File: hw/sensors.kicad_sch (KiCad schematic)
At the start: 0 parts

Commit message: working on documentation, design methmethodology, sizing, layout
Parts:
- added C401, C402, C403, C404: 100nF, Capacitor_SMD:C_0805_2012Metric, symbol Device:C_Small
- added D401, D402, D403, D404: 3.3V Zener, Diode_SMD:D_MiniMELF, symbol Device:D_Zener_Small
- added R401, R402: 2m, Resistor_SMD:R_1206_3216Metric, symbol Device:R
- added R403, R405: 100k, Resistor_SMD:R_0805_2012Metric, symbol Device:R
- added R404: 3k, Resistor_SMD:R_0805_2012Metric, symbol Device:R
- added R406: 2k, Resistor_SMD:R_0805_2012Metric, symbol Device:R
- added TP401, TP405: GND, TestPoint:TestPoint_Pad_1.0x1.0mm, symbol Connector:TestPoint
- added TP402: -ARR, TestPoint:TestPoint_Pad_1.0x1.0mm, symbol Connector:TestPoint
- added TP403: Array Current, TestPoint:TestPoint_Pad_1.0x1.0mm, symbol Connector:TestPoint
- added TP404: -BATT, TestPoint:TestPoint_Pad_1.0x1.0mm, symbol Connector:TestPoint
- added TP406: Battery Current, TestPoint:TestPoint_Pad_1.0x1.0mm, symbol Connector:TestPoint
- added TP407: +ARR, TestPoint:TestPoint_Pad_1.0x1.0mm, symbol Connector:TestPoint
- added TP408: Array Voltage, TestPoint:TestPoint_Pad_1.0x1.0mm, symbol Connector:TestPoint
- added TP409: +BATT, TestPoint:TestPoint_Pad_1.0x1.0mm, symbol Connector:TestPoint
- added TP410: Battery Voltage, TestPoint:TestPoint_Pad_1.0x1.0mm, symbol Connector:TestPoint
- added U401, U402: INA210, Package_TO_SOT_SMD:SOT-363_SC-70-6_Handsoldering, symbol MPPT:OP_AMP_INA21x
- added U403, U404: OPA990, Package_TO_SOT_SMD:SOT-23-6, symbol Amplifier_Operational:MAX4238AUT
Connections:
- new net: R403.1, R404.1, U403.3 (+)
- new net: R405.1, R406.1, U404.3 (+)
- new net +12V: C401.2, C402.2, C403.2, C404.2, U401.3 (V+), U402.3 (V+), U403.6 (V+), U404.6 (V+)
- new net +ARR: R403.2, TP407.1
- new net +BATT: R405.2, TP409.1
- new net -ARR: R401.1, TP402.1, U401.5 (-)
- new net -BATT: R402.2, TP404.1, U402.4 (+)
- new net ARRAY_CURRENT: D401.1 (K), TP403.1, U401.6
- new net ARRAY_VOLTAGE: D403.1 (K), TP408.1, U403.1, U403.4 (-)
- new net BATTERY_CURRENT: D402.1 (K), TP406.1, U402.6
- new net BATTERY_VOLTAGE: D404.1 (K), TP410.1, U404.1, U404.4 (-)
- new net GND: C401.1, C402.1, C403.1, C404.1, D401.2 (A), D402.2 (A), D403.2 (A), D404.2 (A), R401.2, R402.1, R404.2, R406.2, TP401.1, TP405.1, U401.1 (REF), U401.2 (V-), U401.4 (+), U402.1 (REF), U402.2 (V-), U402.5 (-), U403.2 (V-), U403.5 (~{SHDN}), U404.2 (V-), U404.5 (~{SHDN})
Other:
- note added: "0-100V"
- note added: "0-150V"
- note added: "0-3V"
- note added: "7.5A 0-15mV"
- note added: "Array Current Sensor"
- note added: "Array Voltage Sensor"
- note added: "Battery Current Sensor"
- note added: "Battery Voltage Sensor"

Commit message: slight bom updates
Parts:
- C401, U401, U402: In Stock? (none) -> Y
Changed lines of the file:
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@@
+      (effects (font (size 1.27 1.27)) hide)
+    )
+    (property "In Stock?" "Y" (at 69.85 96.52 0)
       (effects (font (size 1.27 1.27)) hide)
     )
@@
       (effects (font (size 1.27 1.27)) hide)
     )
+    (property "In Stock?" "Y" (at 125.73 96.52 0)
+      (effects (font (size 1.27 1.27)) hide)
+    )
     (pin "1")
     (pin "2")
@@
       (effects (font (size 1 1)) hide)
     )
-    (pin "1")
+    (property "In Stock?" "Y" (at 80.01 85.09 0)
+      (effects (font (size 1.27 1.27)) hide)
+    )
+    (pin "1")

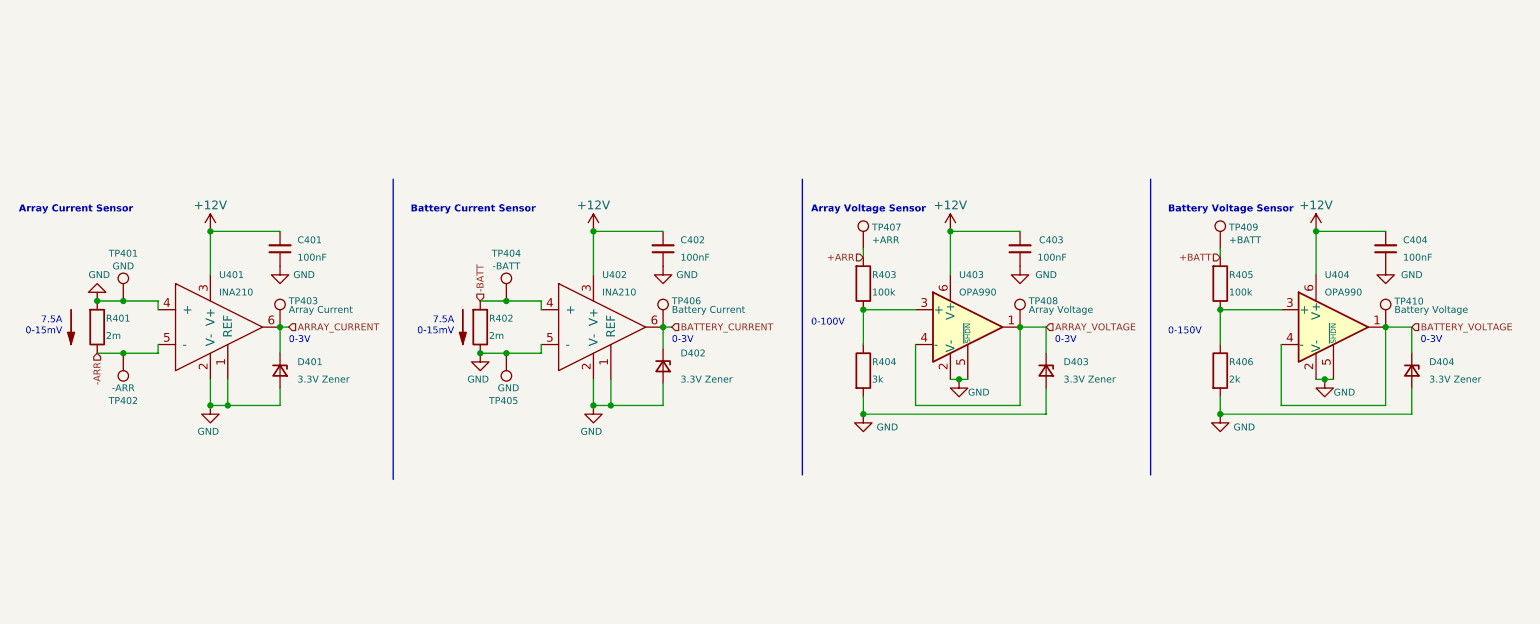
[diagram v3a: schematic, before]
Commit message: revision of PCB layout
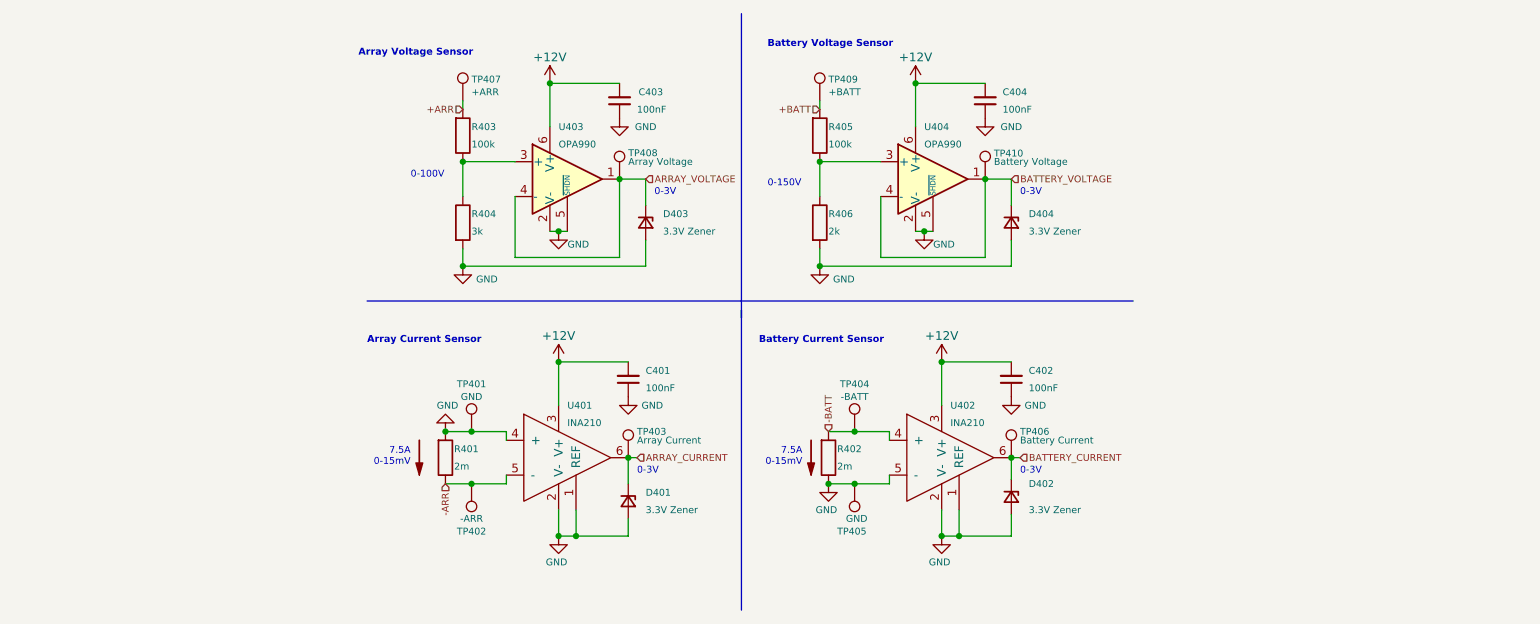
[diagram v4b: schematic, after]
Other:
- moved on the sheet: C401, C402, C403, C404, D401, D402, D403, D404, R401, R402, R403, R404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

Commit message: segregating code into design procedures
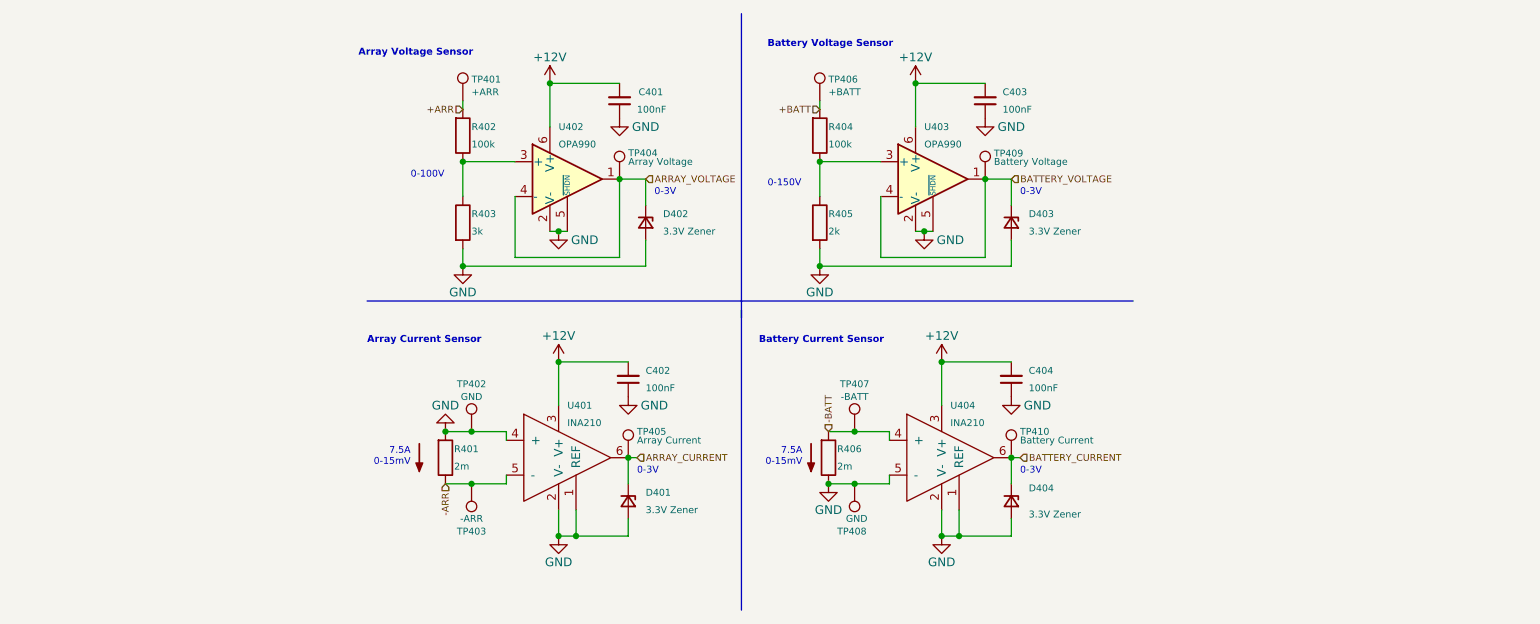
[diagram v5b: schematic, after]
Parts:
- renumbered C403 to C401, C401 to C402, C404 to C403, C402 to C404, D403 to D402, D404 to D403, D402 to D404, R403 to R402, R404 to R403, R405 to R404, R406 to R405, R402 to R406, TP407 to TP401, TP401 to TP402, TP402 to TP403, TP408 to TP404, TP403 to TP405, TP409 to TP406, TP404 to TP407, TP405 to TP408, TP410 to TP409, TP406 to TP410, U403 to U402, U404 to U403, U402 to U404
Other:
- moved on the sheet: D404

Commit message: changed low-speed test points to through-hole standoffs, created a thermal sink area for high-side fet on B.Cu, and changed some thermal resistors to larger 1225 package where available due to lower cost and better thermal resistance
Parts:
- TP401, TP402, TP403, TP404, TP405, TP406, TP407, TP408, TP409, TP410: footprint TestPoint:TestPoint_Pad_1.0x1.0mm -> TestPoint:TestPoint_Keystone_5000-5004_Miniature
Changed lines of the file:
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@@
       (effects (font (size 1 1)) (justify left))
     )
-    (property "Footprint" "TestPoint:TestPoint_Pad_1.0x1.0mm" (at 129.54 74.93 0)
+    (property "Footprint" "TestPoint:TestPoint_Keystone_5000-5004_Miniature" (at 129.54 74.93 0)
       (effects (font (size 1 1)) hide)
     )
@@
       (effects (font (size 1 1)) (justify left))
     )
-    (property "Footprint" "TestPoint:TestPoint_Pad_1.0x1.0mm" (at 191.77 115.57 0)
+    (property "Footprint" "TestPoint:TestPoint_Keystone_5000-5004_Miniature" (at 191.77 115.57 0)
       (effects (font (size 1 1)) hide)
     )
@@
       (effects (font (size 1 1)) (justify left))
     )
-    (property "Footprint" "TestPoint:TestPoint_Pad_1.0x1.0mm" (at 158.75 63.5 0)
+    (property "Footprint" "TestPoint:TestPoint_Keystone_5000-5004_Miniature" (at 158.75 63.5 0)
       (effects (font (size 1 1)) hide)
     )
@@
       (effects (font (size 1 1)))
     )
-    (property "Footprint" "TestPoint:TestPoint_Pad_1.0x1.0mm" (at 107.95 111.76 0)
+    (property "Footprint" "TestPoint:TestPoint_Keystone_5000-5004_Miniature" (at 107.95 111.76 0)
       (effects (font (size 1 1)) hide)
     )
@@
       (effects (font (size 1 1)) (justify left))
     )
-    (property "Footprint" "TestPoint:TestPoint_Pad_1.0x1.0mm" (at 106.68 63.5 0)
+    (property "Footprint" "TestPoint:TestPoint_Keystone_5000-5004_Miniature" (at 106.68 63.5 0)
       (effects (font (size 1 1)) hide)
     )
@@
       (effects (font (size 1 1)) (justify left))
     )
-    (property "Footprint" "TestPoint:TestPoint_Pad_1.0x1.0mm" (at 182.88 74.93 0)
+    (property "Footprint" "TestPoint:TestPoint_Keystone_5000-5004_Miniature" (at 182.88 74.93 0)
       (effects (font (size 1 1)) hide)
     )
@@
       (effects (font (size 1 1)))
     )
-    (property "Footprint" "TestPoint:TestPoint_Pad_1.0x1.0mm" (at 107.95 119.38 0)
+    (property "Footprint" "TestPoint:TestPoint_Keystone_5000-5004_Miniature" (at 107.95 119.38 0)
       (effects (font (size 1 1)) hide)
     )
@@
       (effects (font (size 1 1)) (justify left))
     )
-    (property "Footprint" "TestPoint:TestPoint_Pad_1.0x1.0mm" (at 135.89 115.57 0)
+    (property "Footprint" "TestPoint:TestPoint_Keystone_5000-5004_Miniature" (at 135.89 115.57 0)
       (effects (font (size 1 1)) hide)
     )
@@
       (effects (font (size 1 1)) (justify right))
     )
-    (property "Footprint" "TestPoint:TestPoint_Pad_1.0x1.0mm" (at 163.83 119.38 0)
+    (property "Footprint" "TestPoint:TestPoint_Keystone_5000-5004_Miniature" (at 163.83 119.38 0)
       (effects (font (size 1 1)) hide)
     )
@@
       (effects (font (size 1 1)))
     )
-    (property "Footprint" "TestPoint:TestPoint_Pad_1.0x1.0mm" (at 163.83 111.76 0)
-      (effects (font (size 1 1)) hide)
-    )
+    (property "Footprint" "TestPoint:TestPoint_Keystone_5000-5004_Miniature" (at 163.83 111.76 0)
+      (effects (font (size 1 1)) hide)
+    )

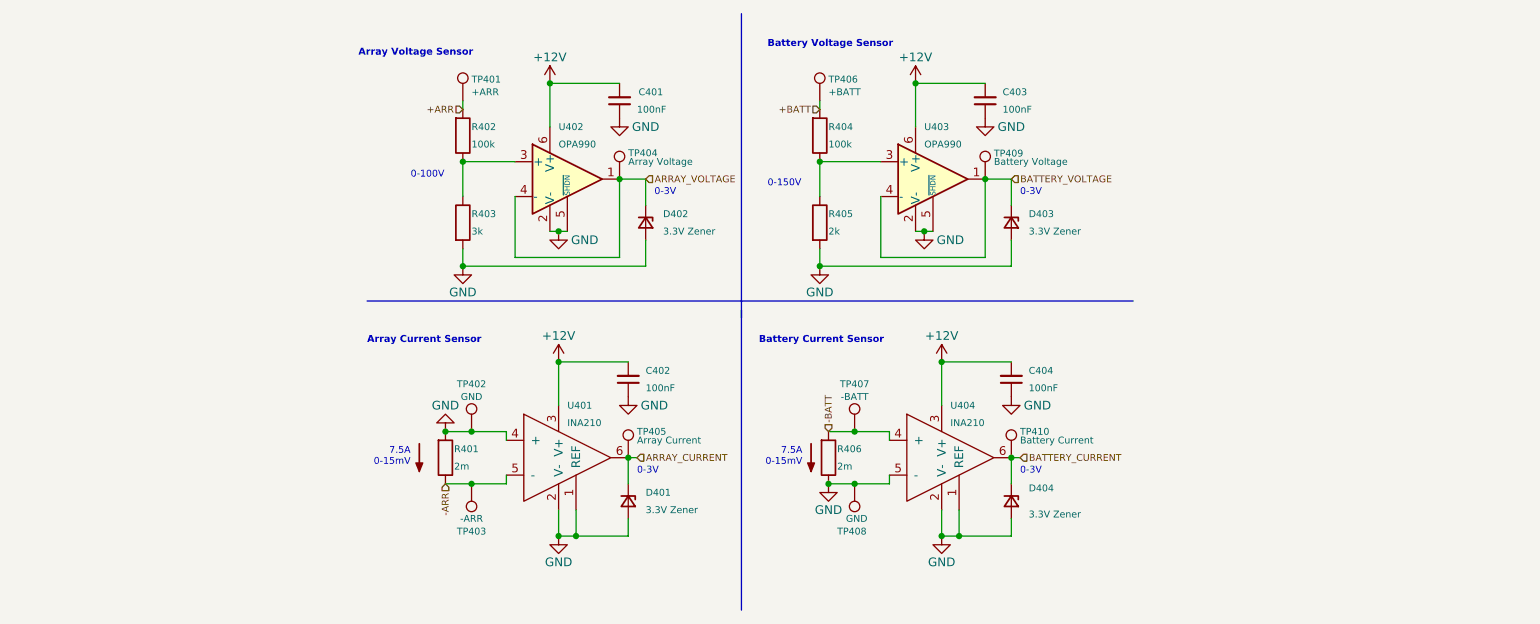
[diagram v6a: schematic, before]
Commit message: rebuild schematic, passes ERC, bom completed
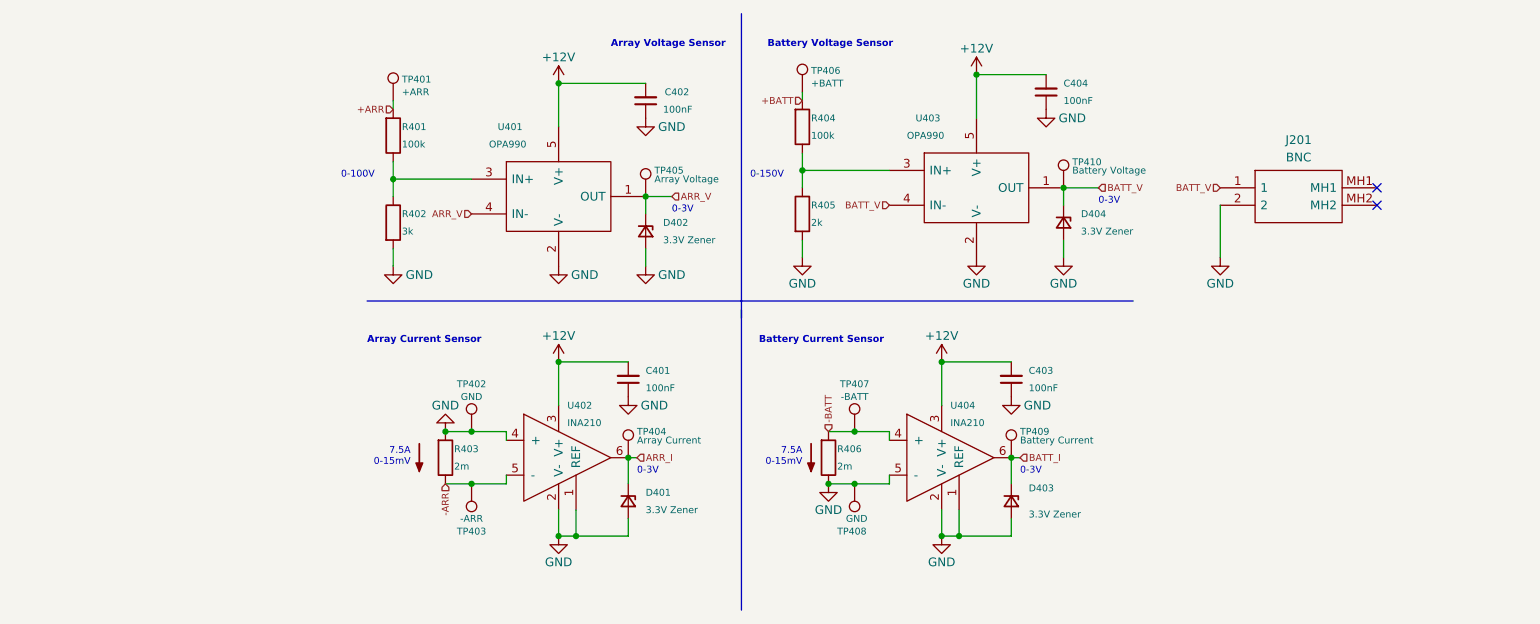
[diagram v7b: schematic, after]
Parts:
- removed D403: 3.3V Zener, Diode_SMD:D_MiniMELF, symbol Device:D_Zener_Small
- removed R403: 3k, Resistor_SMD:R_0805_2012Metric, symbol Device:R
- removed TP404: Array Voltage, TestPoint:TestPoint_Keystone_5000-5004_Miniature, symbol Connector:TestPoint
- removed TP409: Battery Voltage, TestPoint:TestPoint_Keystone_5000-5004_Miniature, symbol Connector:TestPoint
- added D404: 3.3V Zener, Diode_SMD:D_MiniMELF, symbol Device:D_Zener_Small
- added J201: BNC, mppt:CONBNC002, symbol CONBNC002:CONBNC002
- added R401: 100k, Resistor_SMD:R_0805_2012Metric, symbol Device:R
- added TP405: Array Voltage, TestPoint:TestPoint_Keystone_5000-5004_Miniature, symbol Connector:TestPoint
- added TP410: Battery Voltage, TestPoint:TestPoint_Keystone_5000-5004_Miniature, symbol Connector:TestPoint
- C401: renamed from C402; footprint Capacitor_SMD:C_0805_2012Metric -> Capacitor_SMD:C_0402_1005Metric; In Stock? Y -> (none); JLC P/N (none) -> C307331; JLCPCB BOM 1 -> (none); LCSC Part C28233 -> (none); Manufacturer Samsung Elctro-Mechanics -> Samsung Electro-Mechanics; Manufacturer Part Number CL21B104KCFNNNE -> (none); Mouser Part N/A -> (none); P/N (none) -> CL05B104KB54PNC; Projected Cost 0.0083 -> (none); Purchase Page N/A -> (none)
- C402: renamed from C401; footprint Capacitor_SMD:C_0805_2012Metric -> Capacitor_SMD:C_0402_1005Metric; JLC P/N (none) -> C307331; JLCPCB BOM 1 -> (none); LCSC Part C28233 -> (none); Manufacturer Samsung Elctro-Mechanics -> Samsung Electro-Mechanics; Manufacturer Part Number CL21B104KCFNNNE -> (none); Mouser Part N/A -> (none); P/N (none) -> CL05B104KB54PNC; Projected Cost 0.0083 -> (none); Purchase Page N/A -> (none)
- C403: renamed from C404; footprint Capacitor_SMD:C_0805_2012Metric -> Capacitor_SMD:C_0402_1005Metric; JLC P/N (none) -> C307331; JLCPCB BOM 1 -> (none); LCSC Part C28233 -> (none); Manufacturer Samsung Elctro-Mechanics -> Samsung Electro-Mechanics; Manufacturer Part Number CL21B104KCFNNNE -> (none); Mouser Part N/A -> (none); P/N (none) -> CL05B104KB54PNC; Projected Cost 0.0083 -> (none); Purchase Page N/A -> (none)
- C404: renamed from C403; footprint Capacitor_SMD:C_0805_2012Metric -> Capacitor_SMD:C_0402_1005Metric; JLC P/N (none) -> C307331; JLCPCB BOM 1 -> (none); LCSC Part C28233 -> (none); Manufacturer Samsung Elctro-Mechanics -> Samsung Electro-Mechanics; Manufacturer Part Number CL21B104KCFNNNE -> (none); Mouser Part N/A -> (none); P/N (none) -> CL05B104KB54PNC; Projected Cost 0.0083 -> (none); Purchase Page N/A -> (none)
- D401, D402: JLC P/N (none) -> C8056; JLCPCB BOM 1 -> (none); LCSC Part C8056 -> (none); Manufacturer Part Number ZMM3V3-M -> (none); Mouser Part N/A -> (none); P/N (none) -> ZMM3V3-M; Projected Cost 0.0205 -> (none); Purchase Page N/A -> (none)
- D403: renamed from D404; JLC P/N (none) -> C8056; JLCPCB BOM 1 -> (none); LCSC Part C8056 -> (none); Manufacturer Part Number ZMM3V3-M -> (none); Mouser Part N/A -> (none); P/N (none) -> ZMM3V3-M; Projected Cost 0.0205 -> (none); Purchase Page N/A -> (none)
- R402: value 100k -> 3k; JLC P/N (none) -> C17661; JLCPCB BOM 1 -> (none); LCSC Part C149504 -> (none); Manufacturer Part Number 0805W8F1003T5E -> (none); Mouser Part N/A -> (none); P/N (none) -> 0805W8F3001T5E; Projected Cost 0.0025 -> (none); Purchase Page N/A -> (none)
- R403: renamed from R401; Alternative Part https://www.mouser.com/ProductDetail/Bourns/CRF1206-FZ-R002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 -> (none); JLCPCB BOM 0 -> (none); LCSC Part N/A -> (none); Manufacturer Part Number PMR18EZPFV2L00 -> (none); Mouser Part 755-PMR18EZPFV2L00 -> (none); Projected Cost 0.69 -> (none); Purchase Page https://www.mouser.com/ProductDetail/ROHM-Semiconductor/PMR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 -> (none)
- R404: JLC P/N (none) -> C149504; JLCPCB BOM 1 -> (none); LCSC Part C149504 -> (none); Manufacturer Part Number 0805W8F1003T5E -> (none); Mouser Part N/A -> (none); P/N (none) -> 0805W8F1003T5E; Projected Cost 0.0025 -> (none); Purchase Page N/A -> (none)
- R405: JLC P/N (none) -> C17604; JLCPCB BOM 1 -> (none); LCSC Part C17604 -> (none); Manufacturer Part Number 0805W8F2001T5E -> (none); Mouser Part N/A -> (none); P/N (none) -> 0805W8F2001T5E; Projected Cost 0.0025 -> (none); Purchase Page N/A -> (none)
- R406: Alternative Part https://www.mouser.com/ProductDetail/Bourns/CRF1206-FZ-R002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 -> (none); JLCPCB BOM 0 -> (none); LCSC Part N/A -> (none); Manufacturer Part Number PMR18EZPFV2L00 -> (none); Mouser Part 755-PMR18EZPFV2L00 -> (none); Projected Cost 0.69 -> (none); Purchase Page https://www.mouser.com/ProductDetail/ROHM-Semiconductor/PMR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 -> (none)
- TP401, TP406: Color (none) -> Orange; Distributor (none) -> Mouser; Manufacturer (none) -> Keystone Electronics; P/N (none) -> 534-5003
- TP402, TP408: Color (none) -> Black; Distributor (none) -> Mouser; Manufacturer (none) -> Keystone Electronics; P/N (none) -> 534-5001
- TP403, TP407: Color (none) -> Brown; Distributor (none) -> Mouser; Manufacturer (none) -> Keystone Electronics; P/N (none) -> 534-5115
- TP404: renamed from TP405; Color (none) -> Blue; Distributor (none) -> Mouser; Manufacturer (none) -> Keystone Electronics; P/N (none) -> 534-5117
- TP409: renamed from TP410; Color (none) -> Blue; Distributor (none) -> Mouser; Manufacturer (none) -> Keystone Electronics; P/N (none) -> 534-5117
- U401: renamed from U402; footprint Package_TO_SOT_SMD:SOT-23-6 -> mppt:SOT65P210X110-5N; symbol Amplifier_Operational:MAX4238AUT -> OPA990IDCKR:OPA990IDCKR; Alternative Part OPA991, OPA992 -> (none); JLCPCB BOM 0 -> (none); LCSC Part N/A -> (none); Manufacturer Part Number OPA990SIDBVR -> (none); Mouser Part 595-OPA990SIDBVR -> (none); P/N (none) -> 595-OPA990IDCKR; Projected Cost 1.30 -> (none); Purchase Page https://www.mouser.com/ProductDetail/595-OPA990SIDBVR -> (none)
- U402: renamed from U401; In Stock? Y -> (none); JLCPCB BOM 0 -> (none); LCSC Part N/A -> (none); Manufacturer Part Number INA210AIDCKT -> (none); Mouser Part N/A -> (none); P/N (none) -> 595-INA210CQDCKRQ1; Projected Cost 1.156 -> (none); Purchase Page https://www.ti.com/store/ti/en/p/product/?p=INA210AIDCKT&HQ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 -> (none)
- U403: footprint Package_TO_SOT_SMD:SOT-23-6 -> mppt:SOT65P210X110-5N; symbol Amplifier_Operational:MAX4238AUT -> OPA990IDCKR:OPA990IDCKR; Alternative Part OPA991, OPA992 -> (none); JLCPCB BOM 0 -> (none); LCSC Part N/A -> (none); Manufacturer Part Number OPA990SIDBVR -> (none); Mouser Part 595-OPA990SIDBVR -> (none); P/N (none) -> 595-OPA990IDCKR; Projected Cost 1.30 -> (none); Purchase Page https://www.mouser.com/ProductDetail/595-OPA990SIDBVR -> (none)
- U404: In Stock? Y -> (none); JLCPCB BOM 0 -> (none); LCSC Part N/A -> (none); Manufacturer Part Number INA210AIDCKT -> (none); Mouser Part N/A -> (none); P/N (none) -> 595-INA210CQDCKRQ1; Projected Cost 1.156 -> (none); Purchase Page https://www.ti.com/store/ti/en/p/product/?p=INA210AIDCKT&HQ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 -> (none)
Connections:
- net +12V: now also U401.5 (V+), U403.5 (V+); no longer U401.6 (V+), U403.6 (V+)
- net +ARR: now also R401.2; no longer R402.2
- net GND: now also R402.2, D404.2 (A), J201.2; no longer U401.5 (~{SHDN}), U403.5 (~{SHDN})
- net at R402.1, U401.3 (IN+): now also R401.1
- net ARRAY_CURRENT renamed ARR_I
- net ARRAY_VOLTAGE renamed ARR_V
- net ARR_V: now also TP405.1
- net BATTERY_CURRENT renamed BATT_I
- net BATTERY_VOLTAGE renamed BATT_V
- net BATT_V: now also D404.1 (K), J201.1, TP410.1
- no-connect marks 0 -> 2
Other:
- moved on the sheet: C402, C404
